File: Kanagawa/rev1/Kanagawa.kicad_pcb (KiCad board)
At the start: 2 copper layers, 332 x 143 mm, 186 parts, among them J1 Conn_01x04, SW99 Rotary_Encoder_Switch, U0 Elite-C

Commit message: clean revisions
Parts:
- removed MountBaseMiddleTop7, MountBaseMiddleTop8: MountingHole, keyboard:MountingHole_2.2mm_M2_Pad_Via
- KD12: footprint keyboard:SW_Cherry_MX_2.00u_Hotswap -> keyboard:SW_Cherry_MX_2.25u_Hotswap
- KE11: footprint keyboard:SW_Cherry_MX_2.25u_Hotswap -> keyboard:SW_Cherry_MX_1.75u_Hotswap
- KF7, KF9: footprint keyboard:SW_Cherry_MX_1.25u_Hotswap -> keyboard:SW_Cherry_MX_1.00u_Hotswap
- moved MountBaseMiddleTop6 113.3 mm to (383.3, 204.8)
- moved MountBaseMiddleTop5 113.0 mm to (383.0, 82.8)
- moved MountBaseMiddleTop3 48.0 mm to (204.7, 81.8)
- moved MountMiddle0 31.3 mm to (246.2, 84.3)
- moved R2 12.5 mm to (358.0, 81.8)
- moved R1 12.5 mm to (360.7, 81.8)
- moved DE11 11.7 mm to (317.7, 180.7)
- moved DE12 9.74 mm to (346.2, 185.4)
- moved DF10 9.74 mm to (327.2, 204.4)
- moved DF11 9.74 mm to (346.2, 204.3)
- moved DF12 9.74 mm to (365.3, 204.4)
- moved KE12 9.74 mm to (337.8, 180.4)
- moved KF10 9.74 mm to (318.7, 199.4)
- moved KF11 9.74 mm to (337.8, 199.4)
- moved KF12 9.74 mm to (356.8, 199.4)
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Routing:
- net col03: track 386.0 -> 602.9 mm
- net RESET: track 59.3 -> 29.7 mm
- net SDA: track 47.9 -> 66.7 mm, vias 1 -> 3
- net SCL: track 49.9 -> 67.2 mm, vias 1 -> 3
- net col08: track 320.6 -> 303.5 mm
- net Net-(DE11-Pad2): track 15.5 -> 3.46 mm
- net col11: track 260.8 -> 249.9 mm
- net VCC: track 55.7 -> 65.9 mm, vias 1 -> 2
- net col12: track 216.7 -> 208.1 mm
- net col09: track 291.4 -> 283.7 mm
- net row02: track 345.9 -> 353.3 mm
- net col13: track 142.5 -> 135.4 mm
- net row05: track 444.7 -> 437.6 mm
- net col10: track 282.0 -> 276.4 mm
- net col07: track 327.5 -> 324.4 mm
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
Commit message: routing rev1
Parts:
- moved LogoMiddle2 326.5 mm to (73.3, 81.1), turned to 180 degrees
- moved LogoMiddle1 313.8 mm to (83.6, 81.4), turned to 180 degrees
- moved SW99 20.4 mm to (372.2, 115.2)
- moved LogoMiddle0 19.4 mm to (375.7, 194.0)
- moved DE13 19.0 mm to (381.1, 161.5)
- moved DF13 19.0 mm to (381.1, 180.8)
- moved KE13 19.0 mm to (372.7, 156.6)
- moved KF13 19.0 mm to (372.7, 175.6)
- moved DD13 19.0 mm to (381.1, 142.4)
- moved KD13 19.0 mm to (372.7, 137.5)
- moved DA13 13.5 mm to (369.1, 105.7), turned to 0 degrees
- moved R1 6.65 mm to (366.6, 84.9)
- moved R2 6.65 mm to (363.8, 84.9)
- moved J1 5.69 mm to (335.9, 80.9)
- moved MountBaseMiddleTop6 3.45 mm to (379.9, 204.2)
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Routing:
- net RESET: track 29.7 -> 54.2 mm
- net row00: track 432.7 -> 408.9 mm, vias 0 -> 2
- net ENCB: track 33.3 -> 12.9 mm
- net ENCA: track 28.1 -> 9.45 mm
- net row03: track 375.9 -> 367.3 mm
- net col13: track 135.4 -> 142.9 mm, vias 2 -> 1
- net row05: track 437.6 -> 432.0 mm, vias 0 -> 1
- net /SW99B: track 6.42 -> 10.4 mm
- net SDA: track 66.7 -> 64.9 mm, vias 3 -> 1
- net SCL: track 67.2 -> 66.2 mm, vias 3 -> 1
- net VCC: track 65.9 -> 65.2 mm
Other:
- board size 332 x 143 mm -> 328 x 142 mm

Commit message: reviewe kanagawa rev1
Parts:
- removed LogoMiddle0: LOGO, keyboard:Ciaanh_signature_back
- added LogoMiddle: LOGO, keyboard:Cthulhu_logo, B.Cu at (376.9, 195.2)
- J1: footprint keyboard:OLED_128x64_I2C -> keyboard:OLED_128x64_I2C_cutout
- moved LogoMiddle1 249.6 mm to (298.5, 208.3)
- moved LogoMiddle2 249.6 mm to (288.2, 207.9)
- moved MountBaseMiddleTop4 58.4 mm to (244.0, 207.0)
- moved MountBaseMiddleTop3 40.2 mm to (244.9, 81.2)
- moved MountMiddle0 25.3 mm to (220.9, 83.2)
- moved DA13 12.8 mm to (368.9, 92.9)
- moved SW99 10.7 mm to (373.8, 104.6), turned to 90 degrees
- moved RSW0 6.73 mm to (312.7, 78.2)
- moved R1 6.11 mm to (362.0, 80.9)
- moved R2 5.46 mm to (364.9, 79.6)
- moved J1 4.21 mm to (331.9, 79.4)
- moved MountBaseMiddleTop2 3.35 mm to (60.0, 207.0)
- moved MountBaseMiddleTop1 2.92 mm to (60.0, 81.0)
- moved MountBaseMiddleTop6 2.77 mm to (380.0, 207.0)
- moved MountBaseMiddleTop5 2.49 mm to (381.0, 81.0)
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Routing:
- net RESET: track 54.2 -> 71.1 mm
- net ENCB: track 12.9 -> 27.8 mm
- net row00: track 408.9 -> 422.5 mm, vias 2 -> 1
- net col13: track 142.9 -> 153.3 mm
- net SCL: track 66.2 -> 73.7 mm
- net ENCA: track 9.45 -> 14.4 mm
- net VCC: track 65.2 -> 69.8 mm
- net Net-(DE11-Pad2): track 3.46 -> 6.74 mm
- net SDA: track 64.9 -> 66.3 mm
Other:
- board size 328 x 142 mm -> 330 x 144 mm
- board text added: "Kanagawa by Ciaanh - rev1 *prototype*"
- board text removed: "Kanagawa rev 0.1 *prototype*"

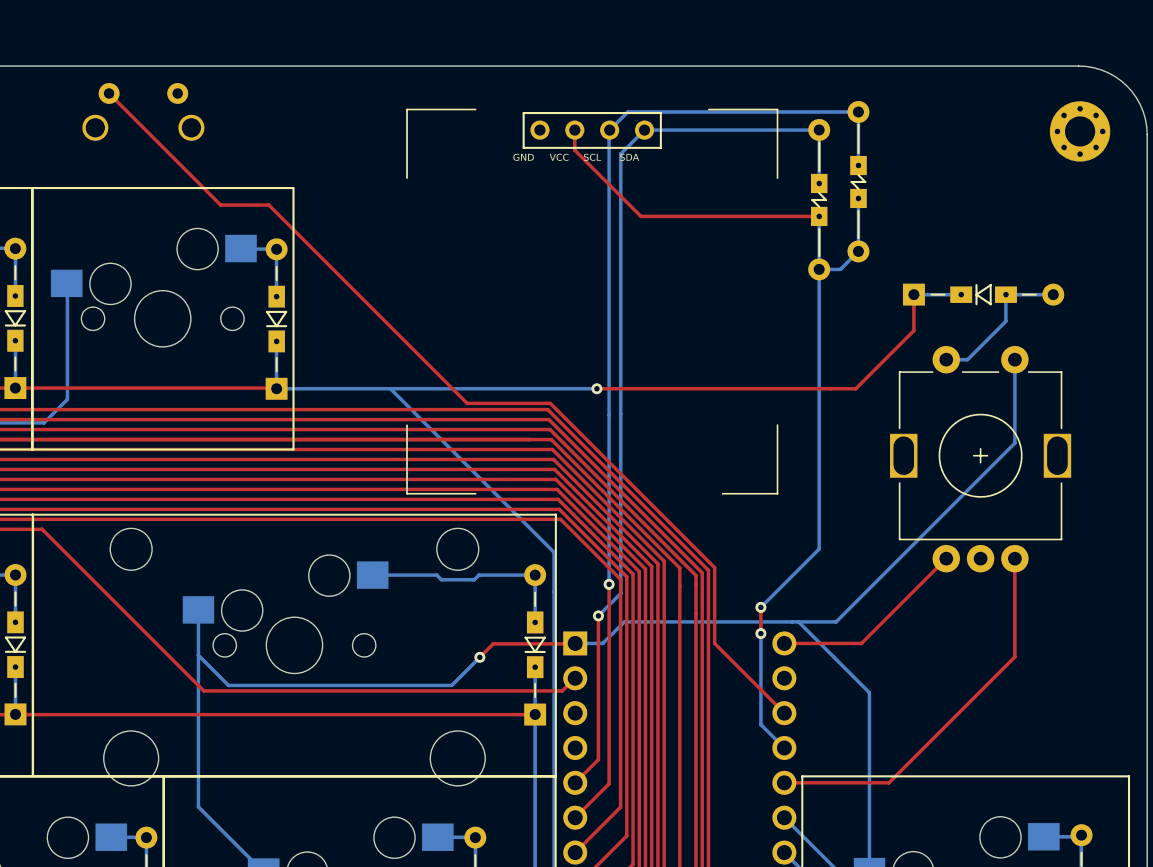
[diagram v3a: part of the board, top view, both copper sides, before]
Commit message: update script pcb generation
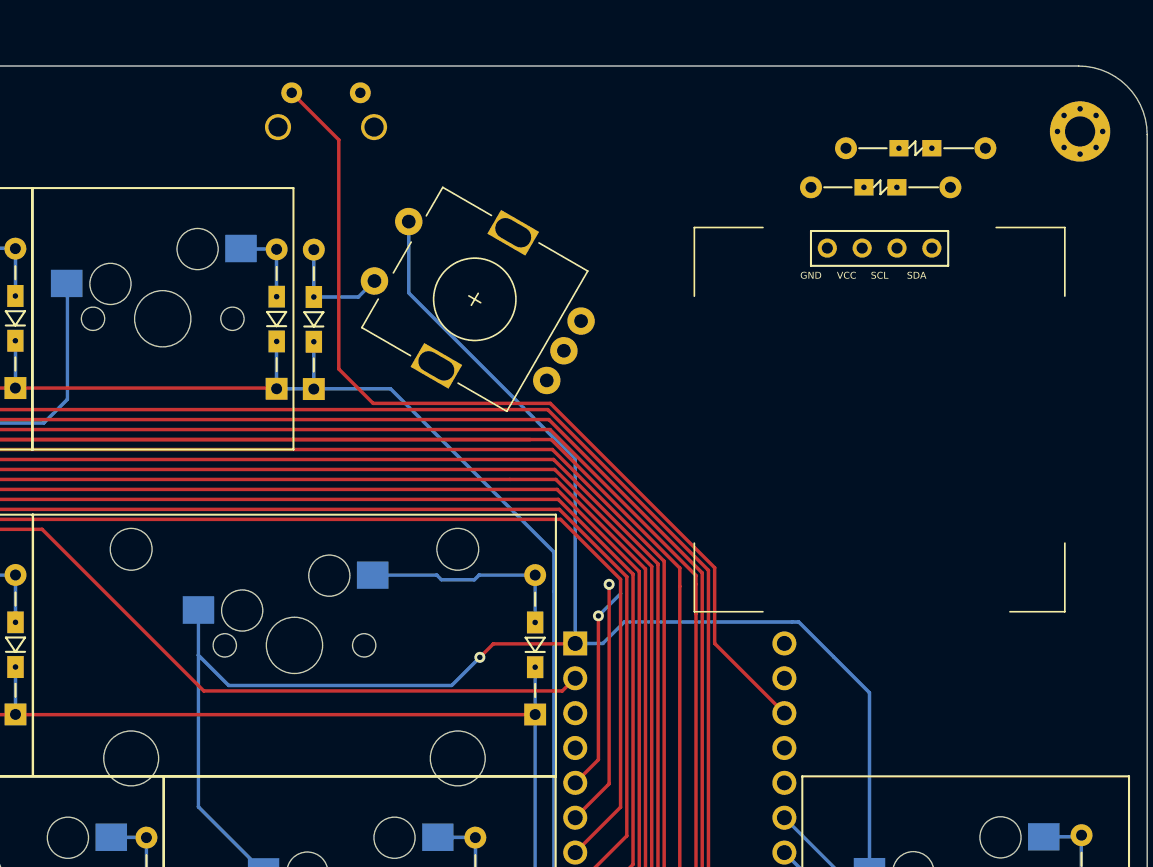
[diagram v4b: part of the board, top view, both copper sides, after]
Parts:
- moved DA13 44.3 mm to (325.2, 99.8), turned to 90 degrees
- moved SW99 38.6 mm to (336.9, 93.2), turned to 150 degrees
- moved J1 22.6 mm to (352.9, 88.0)
- moved RSW0 13.3 mm to (326.1, 78.2)
- moved R1 12.2 mm to (374.1, 82.2), turned to 180 degrees
- moved R2 8.66 mm to (371.6, 85.1), turned to 180 degrees
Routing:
- net VCC: track 69.8 -> 0.09 mm, vias 2 -> 0
- net SCL: track 73.7 -> 18.0 mm
- net SDA: track 66.3 -> 15.2 mm
- net row00: track 422.5 -> 380.0 mm, vias 1 -> 0
- net ENCB: track 27.8 -> 0.00 mm
- net ENCA: track 14.4 -> 0.00 mm
- net col13: track 153.3 -> 161.8 mm
- net RESET: track 71.1 -> 67.6 mm
- net /SW99B: track 10.9 -> 8.35 mm
